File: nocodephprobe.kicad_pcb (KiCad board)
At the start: 2 copper layers, 76 x 80.9 mm, 36 parts, among them J1 RF1-01 BNC, J2 10K, Q1 2N7002, U1 LMV358a, U2 ICL7106CPL, U3 MCP1501T-10E/CHY, U4 VI-302-DP-RC-S, U5 78l05

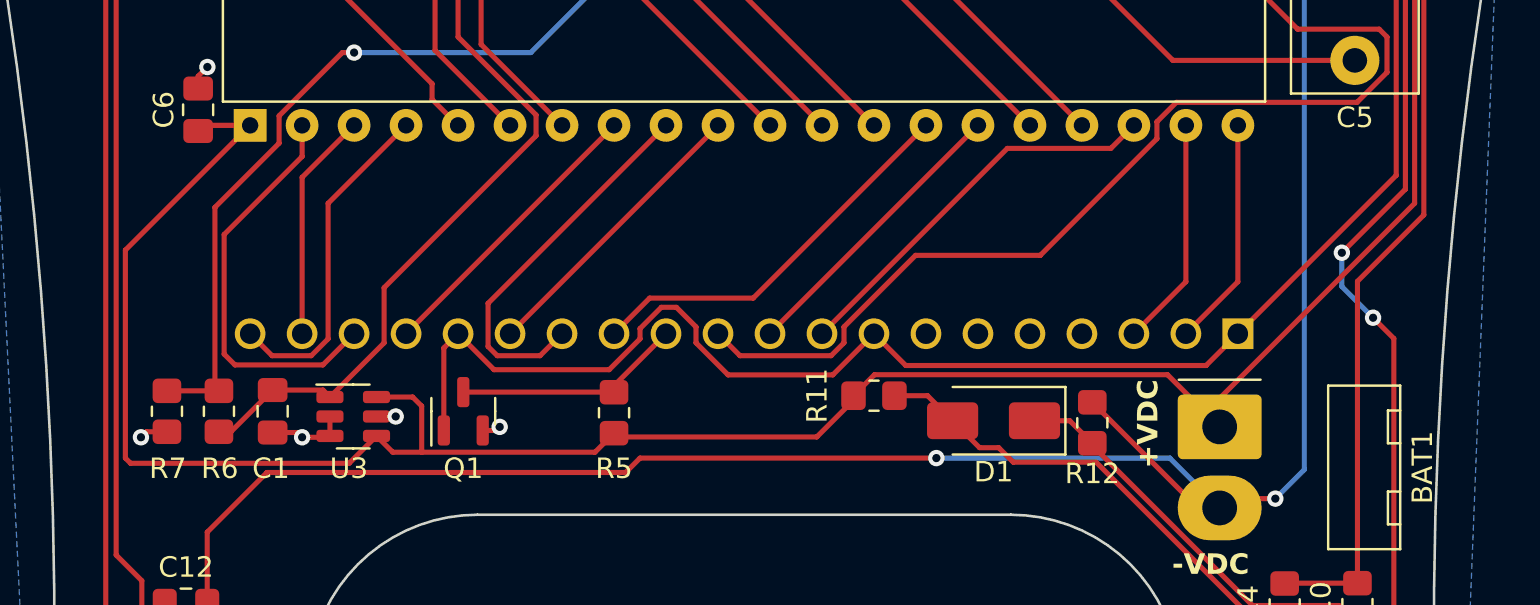
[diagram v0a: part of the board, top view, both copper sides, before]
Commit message: Add header for power switch
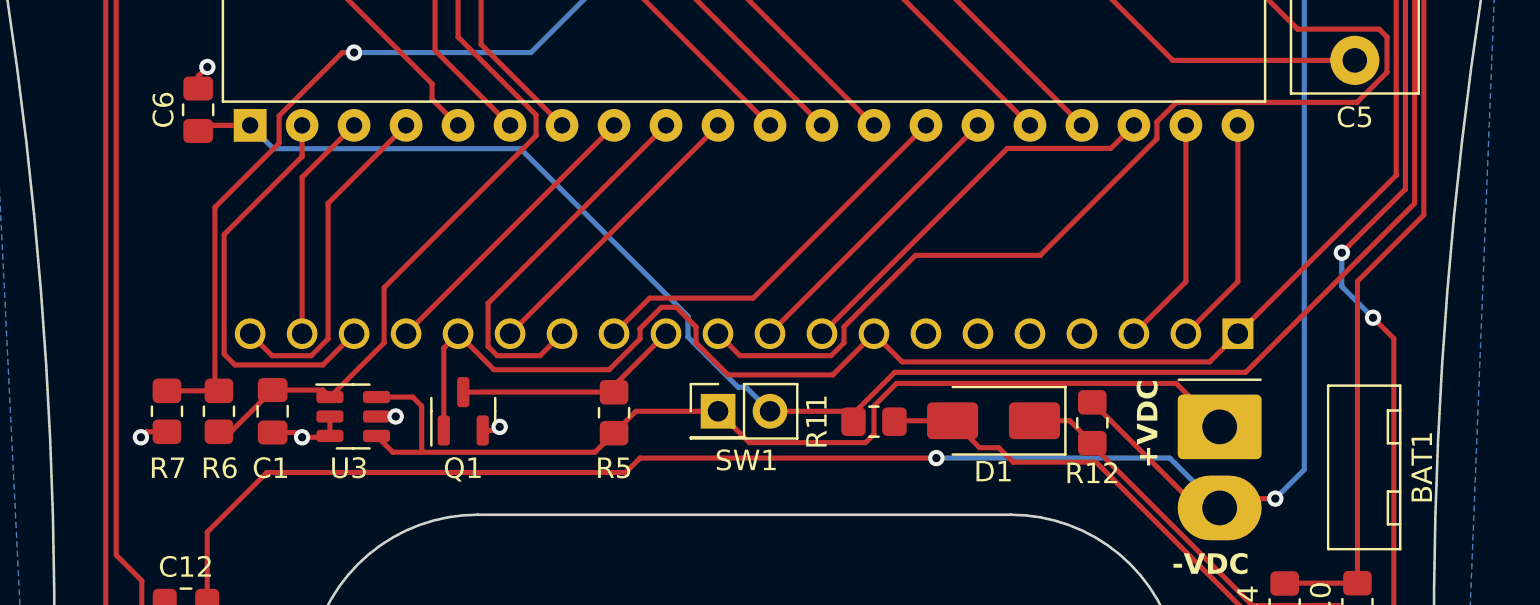
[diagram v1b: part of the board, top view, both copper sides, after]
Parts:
- added SW1: SW_SPST, Connector_PinHeader_2.54mm:PinHeader_2x01_P2.54mm_Vertical, F.Cu at (147.3, 107.2)
- moved R11 1.27 mm to (154.9, 107.7)
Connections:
- C11 pad 2: +VDC -> Net-(SW1-B)
- C6 pad 1: +VDC -> Net-(SW1-B)
- R11 pad 2: +VDC -> Net-(SW1-B)
- U2 pad 1: +VDC -> Net-(SW1-B)
- U5 pad 1: +VDC -> Net-(SW1-B)
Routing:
- net Net-(SW1-B): track 0.00 -> 113.6 mm, vias 0 -> 2
- net +VDC: track 141.1 -> 50.5 mm, vias 2 -> 0

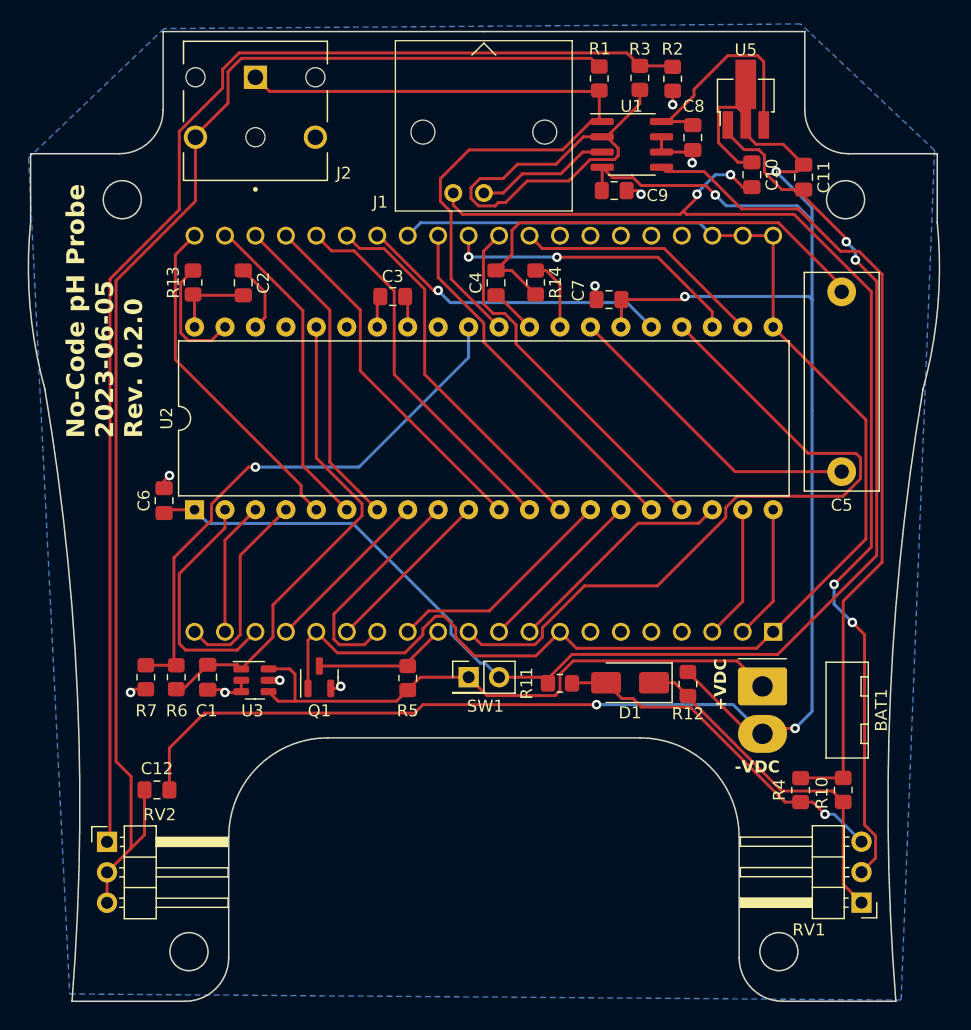
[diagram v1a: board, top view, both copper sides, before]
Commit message: pcb: update PCB to reflect schematic (power 7106 from 5V)
I am really unhappy with the power routing and need to rework the whole
power system so the 7106 can be powered directly from the battery
anyway.
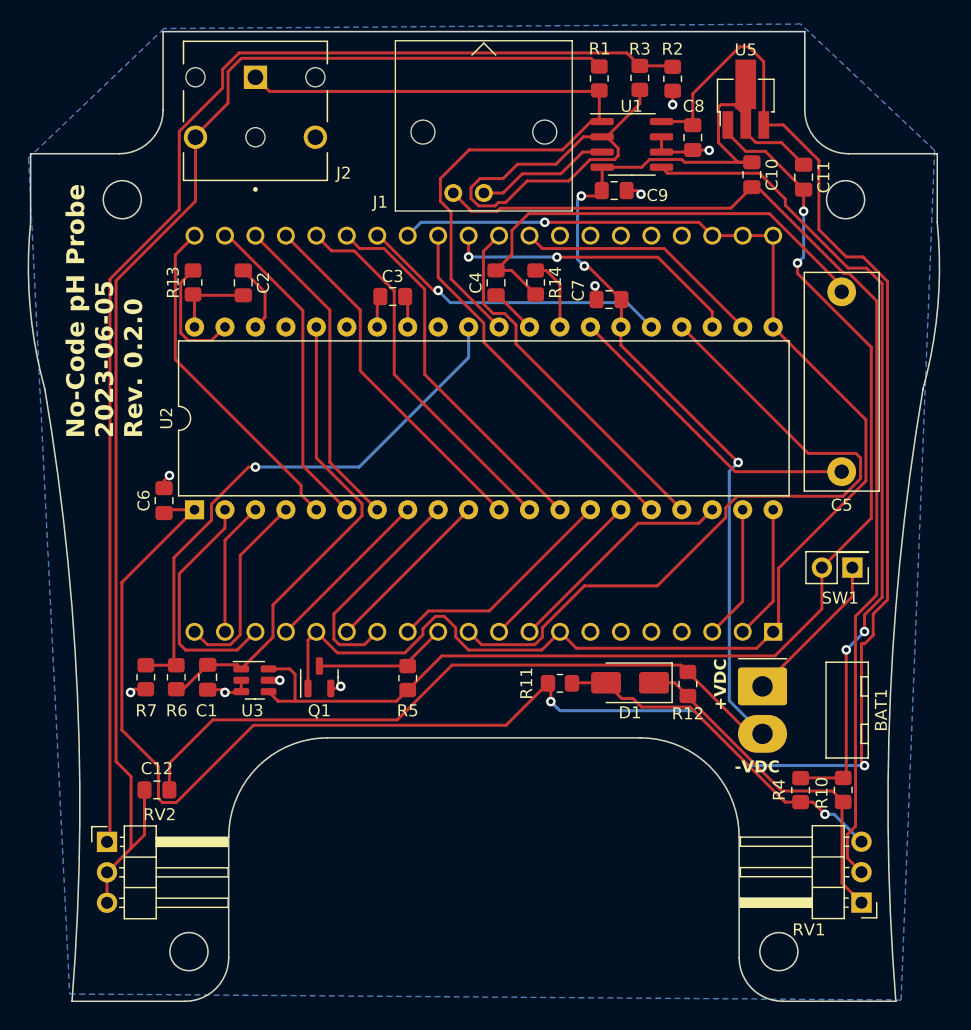
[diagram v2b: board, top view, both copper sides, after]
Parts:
- moved SW1 33.3 mm to (179.3, 98.0), turned to 180 degrees
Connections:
- BAT1 pad 1: +VDC -> Net-(BAT1-+)
- C11 pad 2: Net-(SW1-B) -> +VDC
- C6 pad 1: Net-(SW1-B) -> +5V
- R11 pad 2: Net-(SW1-B) -> +5V
- SW1 pad 1: +VDC -> Net-(BAT1-+)
- SW1 pad 2: Net-(SW1-B) -> +VDC
- U2 pad 1: Net-(SW1-B) -> +5V
- U5 pad 1: Net-(SW1-B) -> +VDC
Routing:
- net +5V: track 19.3 -> 176.6 mm, vias 0 -> 2
- net Net-(SW1-B): track 113.6 -> 0.00 mm, vias 2 -> 0
- net +VDC: track 50.5 -> 102.7 mm, vias 0 -> 2
- net -VDC: track 173.6 -> 142.8 mm, vias 5 -> 3
- net Net-(BAT1-+): track 0.00 -> 13.0 mm
- net Net-(J1-Ext): track 98.3 -> 89.9 mm, vias 4 -> 0
- net Net-(C4-Pad2): track 38.5 -> 39.1 mm
- net BP: track 120.0 -> 119.6 mm, vias 0 -> 1
- net Net-(U1B-+): track 69.0 -> 68.8 mm, vias 0 -> 2

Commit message: pcb: route improved power and headers
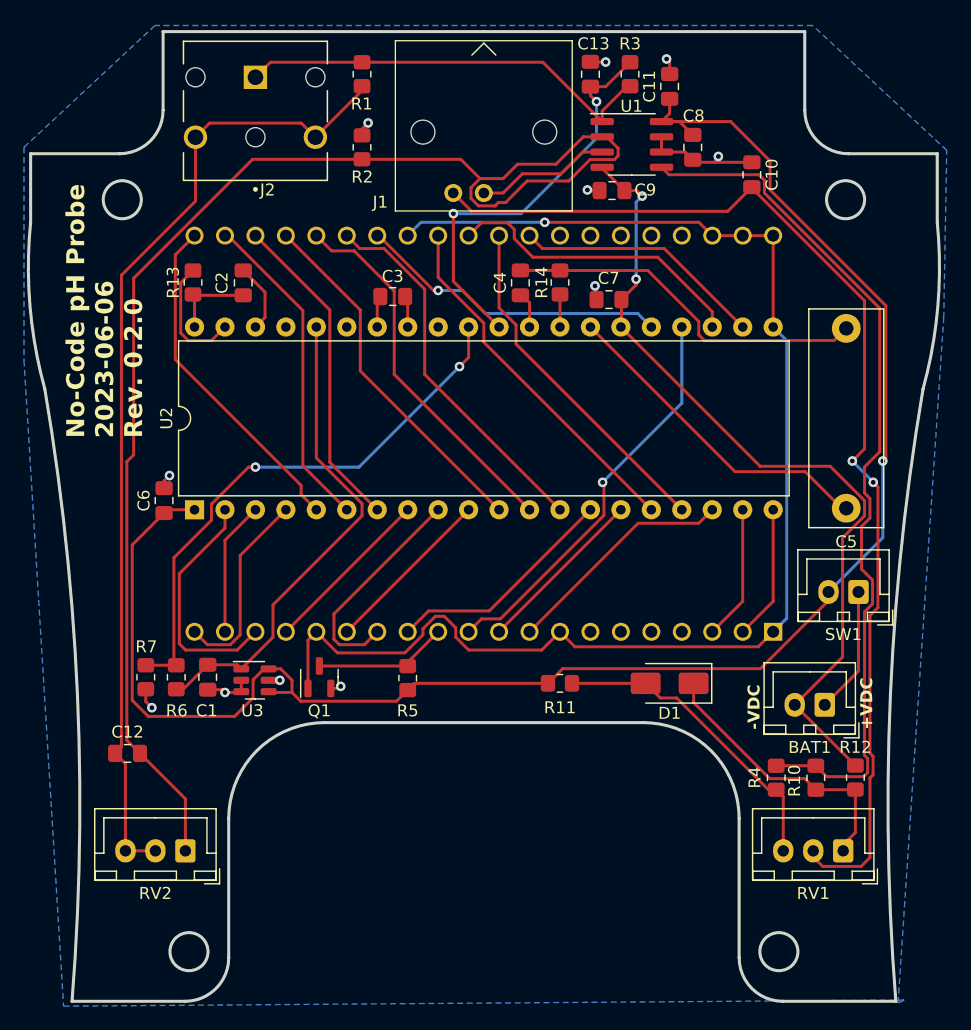
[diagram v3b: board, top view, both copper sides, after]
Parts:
- removed U5: 78l05, Package_TO_SOT_SMD:SOT-89-3_Handsoldering
- added C13: 0.1uF, Capacitor_SMD:C_0805_2012Metric_Pad1.18x1.45mm_HandSolder, F.Cu at (157.5, 56.9)
- BAT1: footprint Connector_Molex:Molex_KK-396_A-41792-0002_1x02_P3.96mm_Horizontal -> Connector_JST:JST_XH_B2B-XH-A_1x02_P2.50mm_Vertical
- C11: value 0.33uF -> 0.1uF
- R3: value 50M -> 10k
- RV1, RV2: footprint Connector_PinHeader_2.54mm:PinHeader_1x03_P2.54mm_Horizontal -> Connector_JST:JST_XH_B3B-XH-A_1x03_P2.50mm_Vertical
- SW1: footprint Connector_PinHeader_2.54mm:PinHeader_2x01_P2.54mm_Vertical -> Connector_JST:JST_XH_B2B-XH-A_1x02_P2.50mm_Vertical
- U1: value LMV358a -> TLV272
- moved R2 26.5 mm to (138.4, 63.0), turned to -90 degrees
- moved R1 19.8 mm to (138.4, 56.9), turned to 90 degrees
- moved R12 16.0 mm to (179.6, 115.6)
- moved C11 13.5 mm to (164.1, 57.9), turned to 90 degrees
- moved RV2 6.58 mm to (123.7, 121.7), turned to 180 degrees
- moved BAT1 5.41 mm to (177.0, 109.5), turned to 180 degrees
- moved RV1 4.58 mm to (178.6, 121.7)
- moved C12 3.91 mm to (118.9, 113.5)
- moved D1 3.30 mm to (164.1, 107.7)
- moved C5 3.07 mm to (178.8, 93.1)
- moved R10 2.50 mm to (176.3, 115.6)
- moved R4 2.28 mm to (173.0, 115.6)
- moved SW1 2.09 mm to (179.8, 100.1)
- moved C4 2.03 mm to (151.6, 74.3)
- moved R14 2.03 mm to (154.9, 74.3), turned to 90 degrees
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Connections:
- C10 pad 1: -VDC -> GND
- C11 pad 1: -VDC -> +VDC
- C11 pad 2: +VDC -> GND
- C12 pad 1: -VDC -> Net-(U1A--)
- C6 pad 1: +5V -> +VDC
- C8 pad 1: +5V -> +VDC
- J2 pad 2: (no net) -> Net-(C12-Pad2)
- R11 pad 2: +5V -> +VDC
- R2 pad 2: Net-(R2-Pad2) -> Net-(U1A--)
- R3 pad 1: Net-(U1A--) -> /scaled
- R3 pad 2: Net-(R2-Pad2) -> Net-(U2-IN_LO)
- RV2 pad 1: Net-(R2-Pad2) -> Net-(U1A--)
- U1 pad 8: +5V -> +VDC
- U2 pad 1: +5V -> +VDC
- U2 pad 30: /scaled -> Net-(U2-IN_LO)
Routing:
- net +5V: track 176.6 -> 0.00 mm, vias 2 -> 0
- net Net-(R2-Pad2): track 106.7 -> 0.00 mm
- net Net-(U1A--): track 35.3 -> 113.9 mm
- net -VDC: track 142.8 -> 69.0 mm, vias 3 -> 2
- net +VDC: track 102.7 -> 146.0 mm, vias 2 -> 1
- net Net-(U2-IN_LO): track 0.00 -> 34.2 mm, vias 0 -> 2
- net Net-(C12-Pad2): track 111.6 -> 82.0 mm
- net Net-(U2-C3): track 61.0 -> 33.8 mm, vias 0 -> 1
- net /scaled: track 61.8 -> 35.5 mm
- net Net-(C4-Pad2): track 39.1 -> 30.7 mm
- net GND: track 17.3 -> 24.6 mm, vias 9 -> 11
- net BP: track 119.6 -> 114.1 mm
- net Net-(D1-K): track 28.8 -> 23.9 mm
- net Net-(J1-Ext): track 89.9 -> 94.1 mm, vias 0 -> 2
- net Net-(D1-A): track 29.7 -> 25.5 mm, vias 1 -> 0
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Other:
- outline, holes or cut-outs redrawn

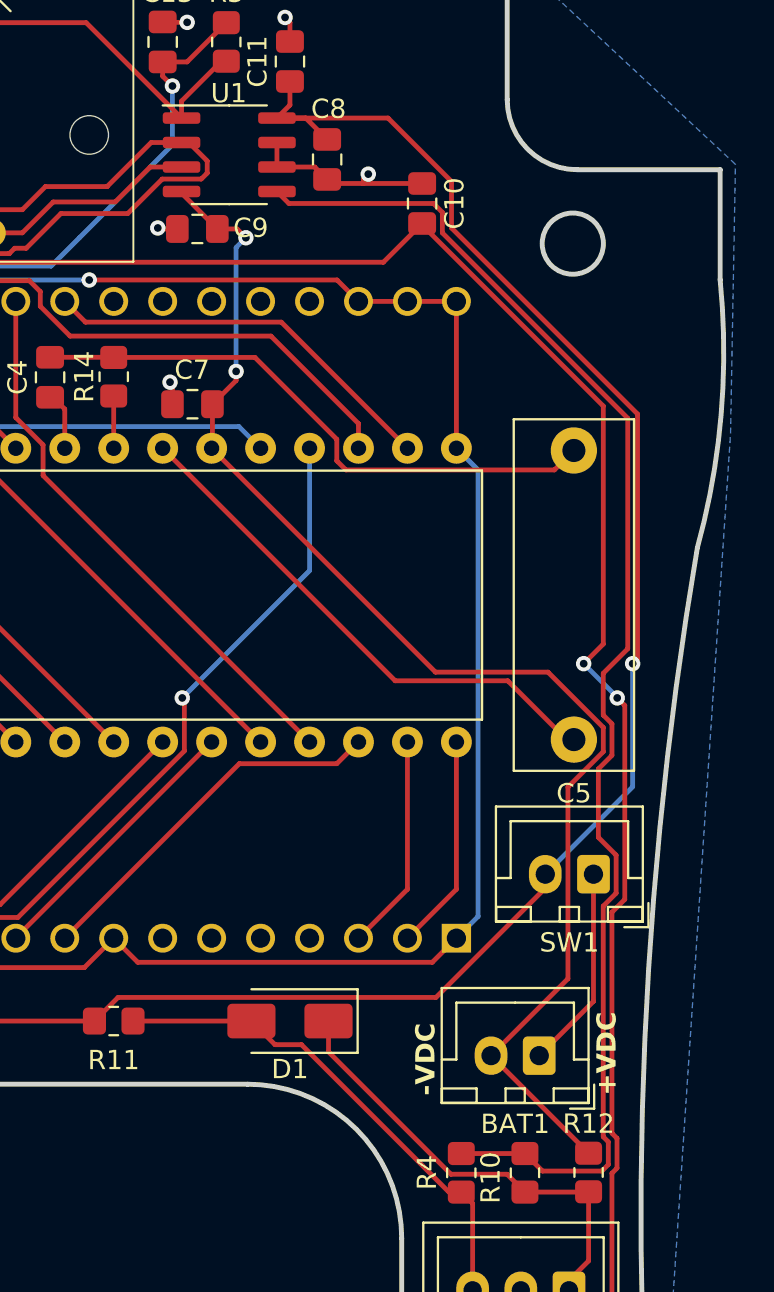
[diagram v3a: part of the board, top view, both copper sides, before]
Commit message: pcb: move switch header to above C5
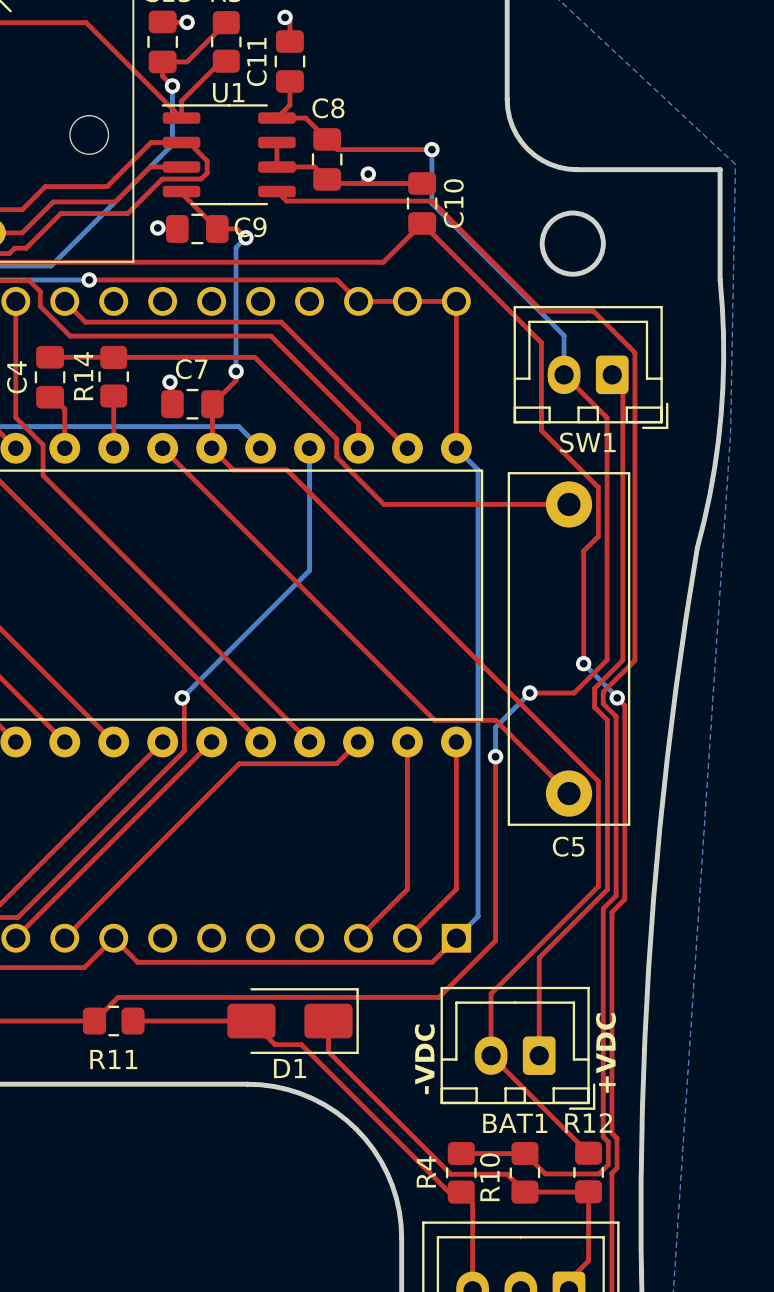
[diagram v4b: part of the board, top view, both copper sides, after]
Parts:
- moved SW1 25.9 mm to (180.8, 74.2)
- moved C5 2.81 mm to (178.6, 95.9)
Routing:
- net Net-(BAT1-+): track 10.6 -> 37.9 mm
- net +VDC: track 146.0 -> 143.4 mm, vias 1 -> 3
- net -VDC: track 69.0 -> 67.0 mm
- net Net-(U1B-+): track 72.3 -> 73.8 mm
- net Net-(U2-INT): track 27.8 -> 28.5 mm

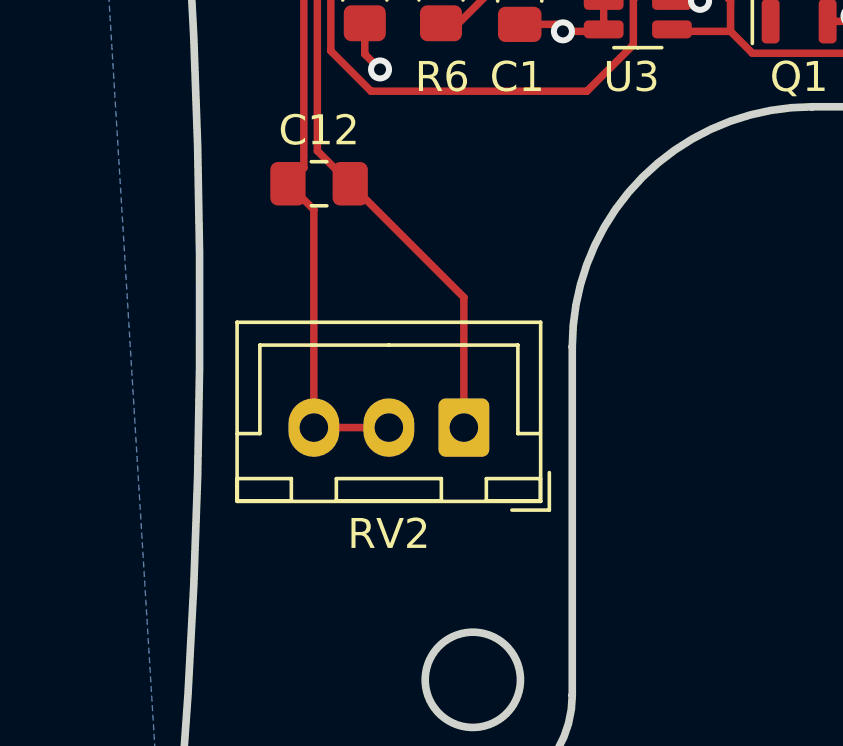
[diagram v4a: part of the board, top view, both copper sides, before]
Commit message: pcb: use 2-pin header for RV2
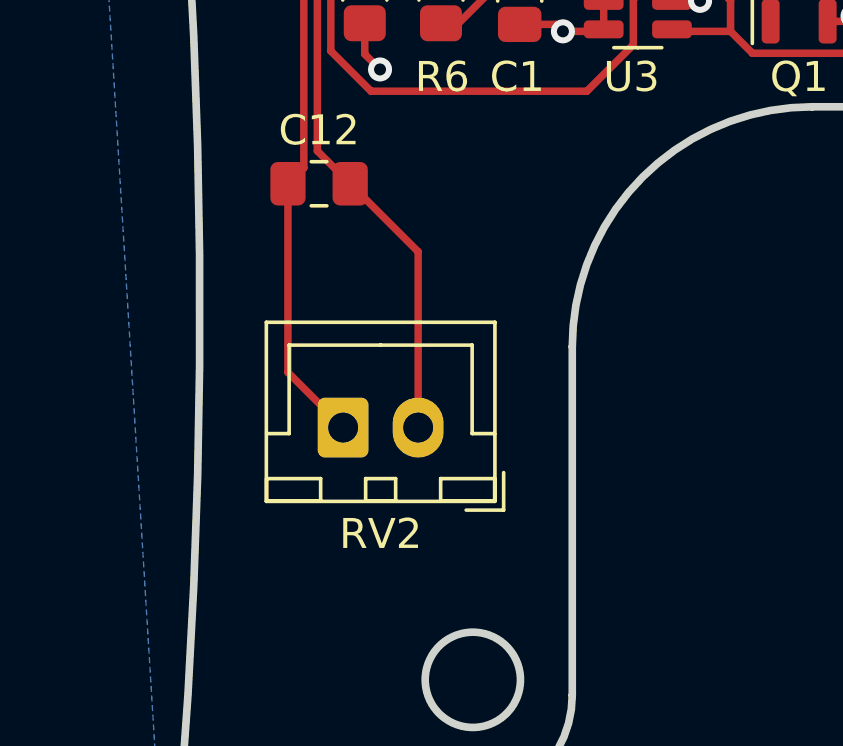
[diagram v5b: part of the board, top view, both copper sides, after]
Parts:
- J1: value RF1-01 BNC -> BNC (pH Probe)
- RV2: footprint Connector_JST:JST_XH_B3B-XH-A_1x03_P2.50mm_Vertical -> Connector_JST:JST_XH_B2B-XH-A_1x02_P2.50mm_Vertical
- moved RV2 1.52 mm to (122.2, 121.7)
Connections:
- RV2 pad 1: Net-(U1A--) -> Net-(C12-Pad2)
- RV2 pad 2: Net-(C12-Pad2) -> Net-(U1A--)
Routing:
- net Net-(C12-Pad2): track 82.0 -> 79.9 mm
- net Net-(U1A--): track 113.9 -> 113.3 mm
